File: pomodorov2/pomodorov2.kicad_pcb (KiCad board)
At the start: 2 copper layers, 32.8 x 23.8 mm, 27 parts, among them J1 USB_B_Micro, J2 TC2050-IDC, J3 SOICbite, J4 Stemma, U1 MDBT50Q-1MV2, Y1 32.768kHz, Y1 32MHz, Y2 32.768kHz

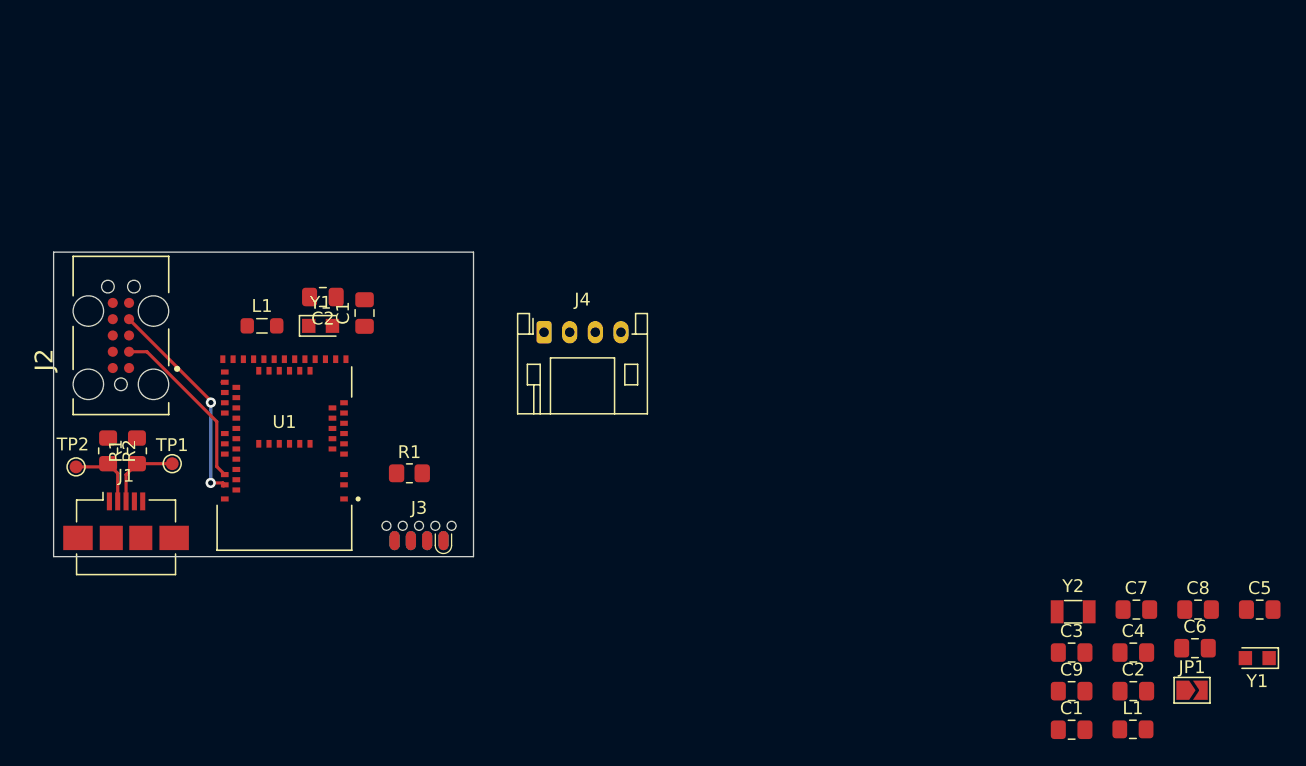
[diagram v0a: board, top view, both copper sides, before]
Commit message: Populate parts on board, remove stemma conn 🪓
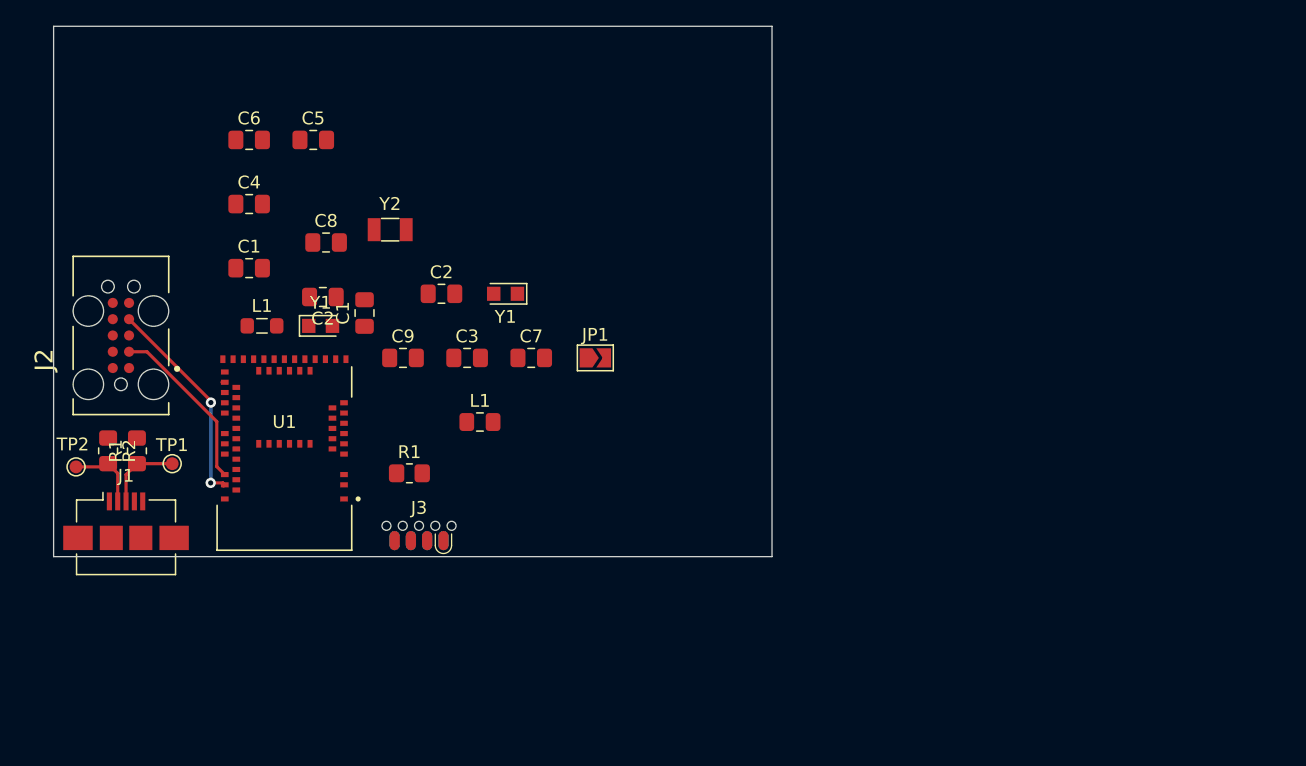
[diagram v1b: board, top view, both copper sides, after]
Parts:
- removed J4: Stemma, Connector_JST:JST_PH_S4B-PH-K_1x04_P2.00mm_Horizontal
- moved C6 83.7 mm to (104.0, 81.0)
- moved C5 82.4 mm to (109.0, 81.0)
- moved C4 77.3 mm to (104.0, 86.0)
- moved C8 73.8 mm to (110.0, 89.0)
- moved C1 73.6 mm to (104.0, 91.0)
- moved Y1 65.1 mm to (124.0, 93.0)
- moved C2 62.2 mm to (119.0, 93.0)
- moved Y2 61.0 mm to (115.0, 88.0)
- moved C9 58.3 mm to (116.0, 98.0)
- moved L1 56.3 mm to (122.0, 103.0)
- moved JP1 53.3 mm to (131.0, 98.0)
- moved C3 52.5 mm to (121.0, 98.0)
- moved C7 51.1 mm to (126.0, 98.0)
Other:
- board size 32.8 x 23.8 mm -> 56 x 41.4 mm
